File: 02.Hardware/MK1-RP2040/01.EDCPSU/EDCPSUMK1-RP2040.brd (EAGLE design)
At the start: 96 x 53.1 mm, 182 parts, among them J6 Display, Q2 2N7002PW, Q4 2N7002PW, Q9 2N7002PW, U1 RP2040TR7, U11 AP63203, U12 AP64501SP-13, U2 MCP4725, U3 SN74AC14PWR, U4 MAX9938FEUK+T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

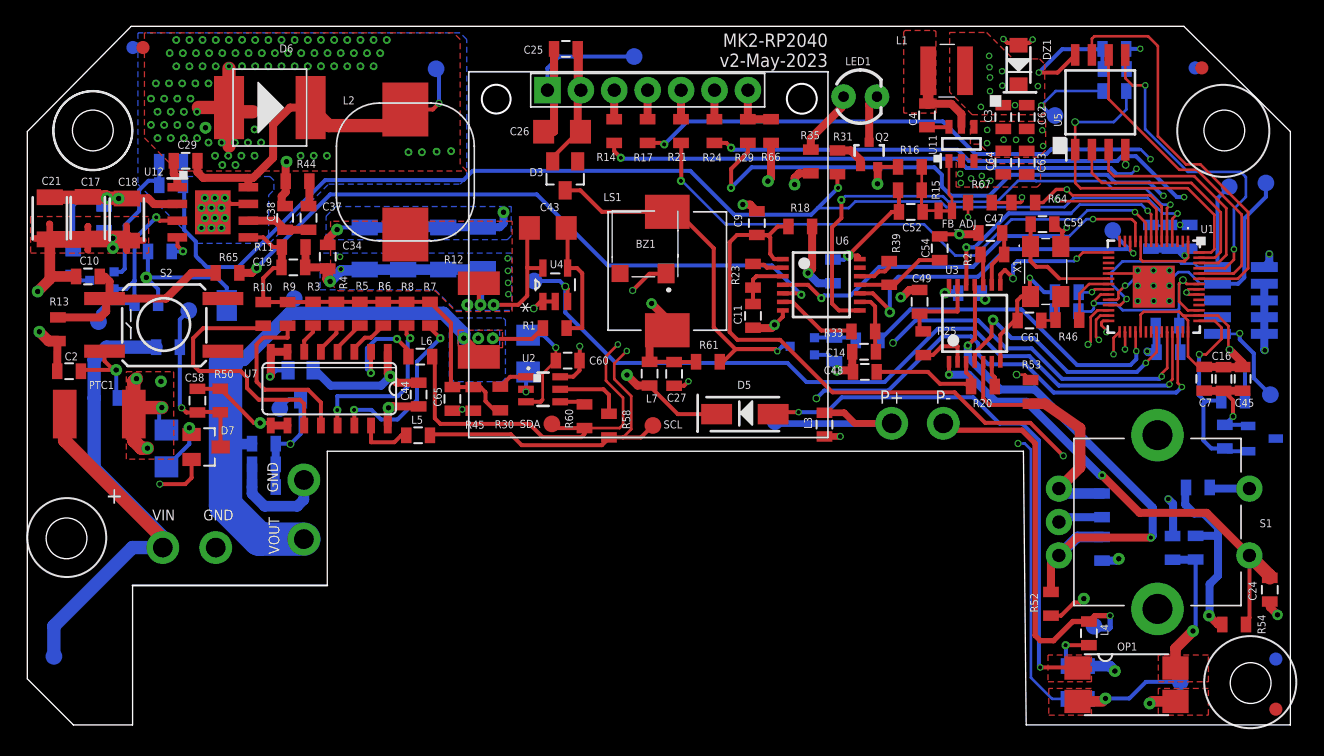
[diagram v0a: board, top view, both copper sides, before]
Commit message: Actualizacion BOM MK1 RP2040 y cambios menores
Se agranda los agujeros laterales del rotary.
Intercambio de posición de las vías del pedal.
Acortamiento de la peninsula.
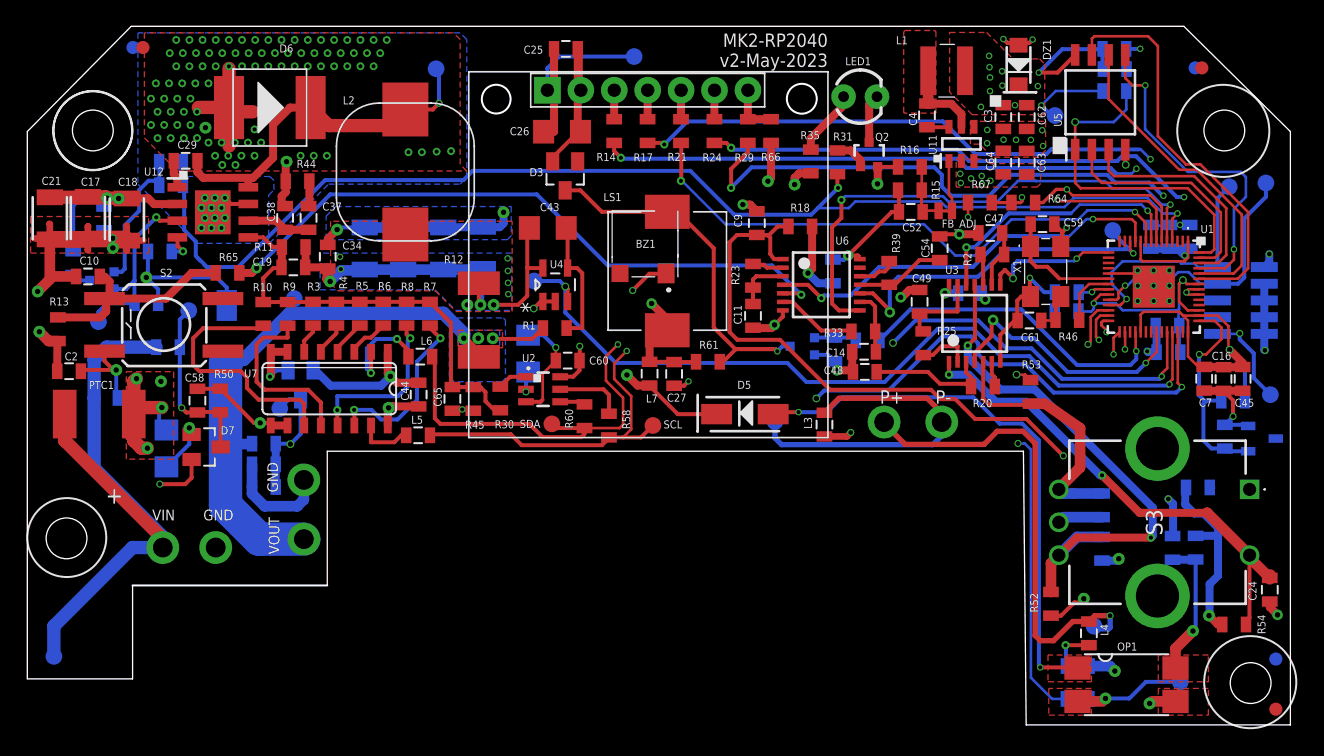
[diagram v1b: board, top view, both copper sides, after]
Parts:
- removed S1: ROTARTY_ENCODER, SparkFun-Electromechanical:ROTARY_ENC_PLAIN
- added S3: PEC12R-3220F-S0024, PEC12R-3220F-S0024:PEC12R3220FS0024
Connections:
- net GND: now also S3.1, S3.C1; no longer S1.C, S1.SW-
- net ROTA: now also S3.A1; no longer S1.A
- net ROTB: now also S3.B1; no longer S1.B
- net ROTPUSH: now also S3.2; no longer S1.SW+
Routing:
- net PEDAL+: track 14.4 -> 26.0 mm
- net PEDAL-: track 31.1 -> 36.5 mm
- net GND: track 210.9 -> 208.0 mm
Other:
- outline, holes or cut-outs redrawn

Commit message: Cierra issue #2 y revision general para peticion de fabricacion SETI
Revision general.
Se añade detalles menores.
Cierra issue #2
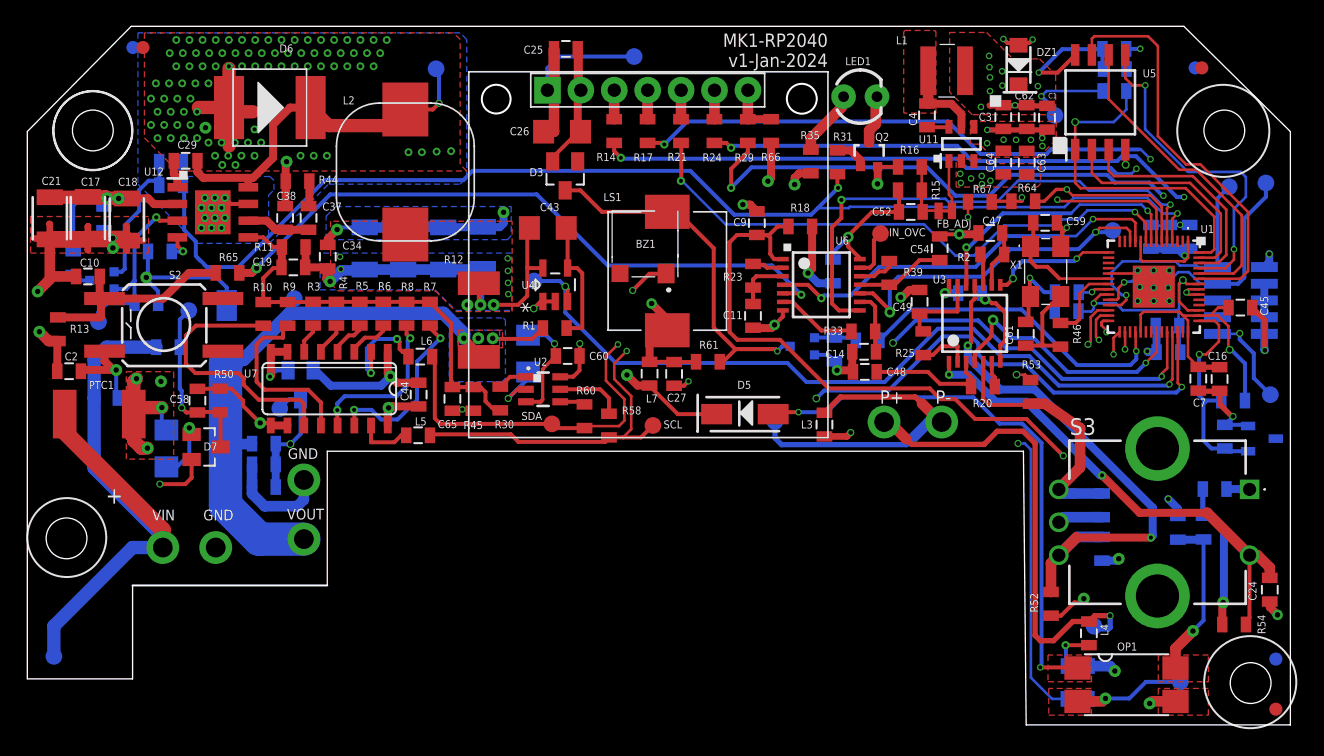
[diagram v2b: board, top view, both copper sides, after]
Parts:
- added C1: 100n 50v X7R/X5R, SparkFun-Passives:0805
- added IN_OVC: TESTPAD_TPSQB1,27, BeagleBone_Blue_R3:TESTPAD_B1,27
- moved C45 5.42 mm to (107.0, 51.4), turned to 0 degrees
- moved R19 1.64 mm to (104.2, 34.7)
- moved R99 1.58 mm to (102.2, 34.7)
- moved C12 1.28 mm to (105.0, 37.6)
- moved R46 1.23 mm to (93.3, 49.4), turned to 270 degrees
- moved C61 1.05 mm to (90.7, 49.4), turned to 270 degrees
- moved C7 0.45 mm to (103.8, 46.0)
- moved C60 0.35 mm to (55.9, 47.7)
- moved C16 0.30 mm to (105.4, 46.0)
- moved C59 0.22 mm to (92.2, 57.9)
- moved R64 0.10 mm to (90.5, 59.5)
- moved R67 0.05 mm to (87.2, 59.5)
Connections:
- net 3V3MCU: now also C1.2
- net GND: now also C1.1
- net IN_OVC: now also IN_OVC.TP
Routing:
- net GND: track 208.0 -> 222.2 mm
- net N$63: track 3.26 -> 7.26 mm
- net IN_OVC: track 0.00 -> 3.71 mm
- net SDA: track 92.4 -> 88.9 mm
- net ROTB: track 44.3 -> 41.3 mm
- net PEDAL: track 10.6 -> 12.6 mm
- net XOUT: track 4.53 -> 6.07 mm
- net PDL: track 56.9 -> 55.5 mm
- net ROTB_FILT: track 10.9 -> 9.62 mm
- net 3V3MCU: track 148.8 -> 149.9 mm
- net N$9: track 19.5 -> 20.5 mm
- net PEDAL+: track 26.0 -> 25.1 mm
- net OVC_ALARM: track 28.2 -> 27.5 mm
- net SS: track 61.5 -> 60.8 mm
- net N$17: track 16.5 -> 15.9 mm
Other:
- board text added: "MK1-RP2040 v1-Jan-2024"
- board text removed: "MK2-RP2040 v2-May-2023"

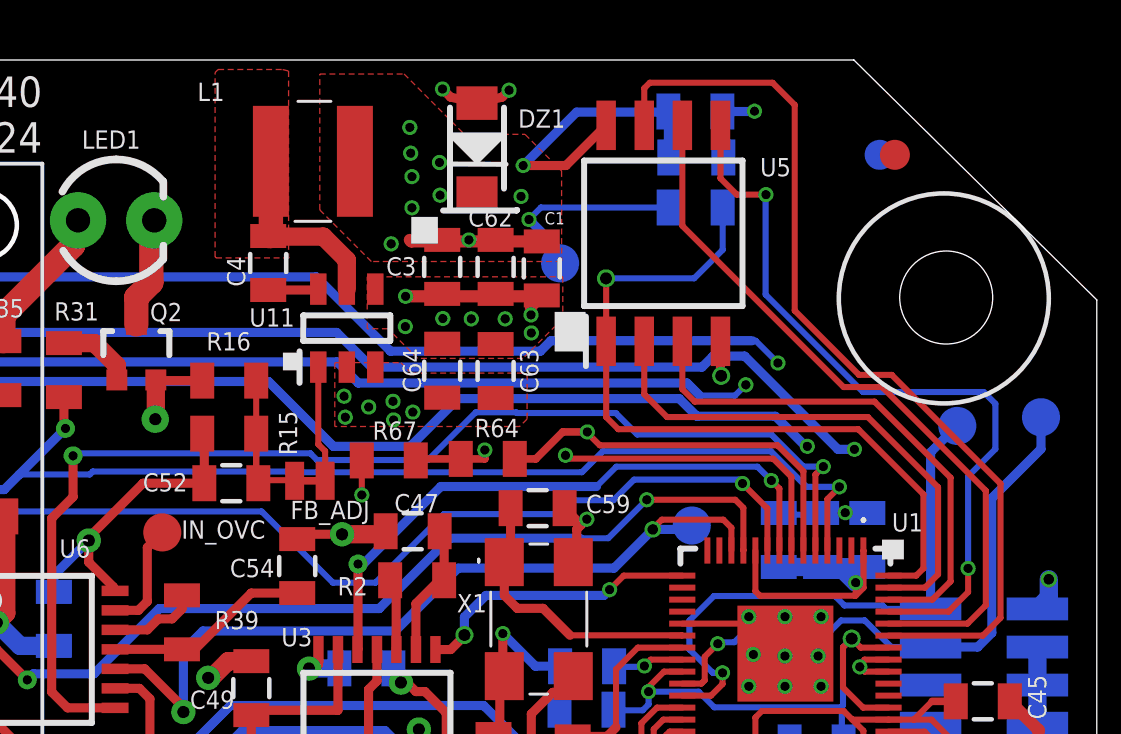
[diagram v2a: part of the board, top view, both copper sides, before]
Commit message: PCB MK1 RP2040- Pines RX TX
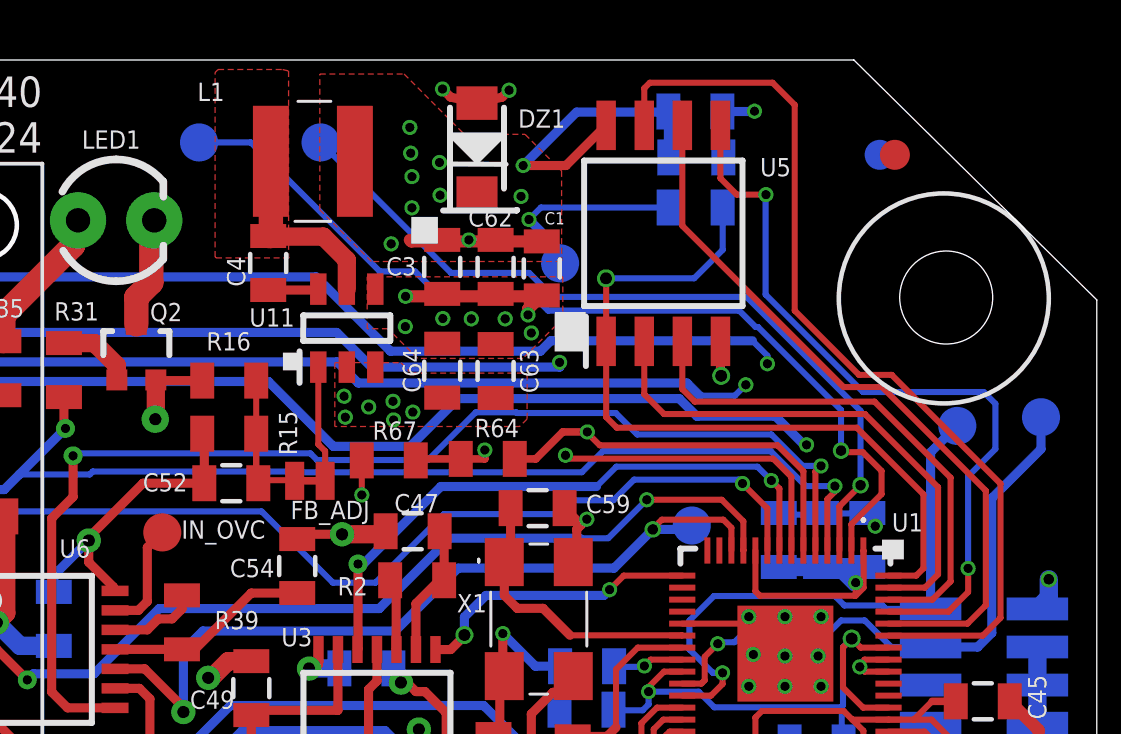
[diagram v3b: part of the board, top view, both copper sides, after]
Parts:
- added RX, TX: TESTPAD_TPSQB1,27, BeagleBone_Blue_R3:TESTPAD_B1,27
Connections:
- net RX: now also RX.TP
- net TX: now also TX.TP
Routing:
- net TX: track 0.00 -> 31.1 mm, vias 0 -> 1
- net RX: track 0.00 -> 26.7 mm, vias 0 -> 1
- net GND: track 222.2 -> 223.2 mm
- net MISO: track 58.5 -> 57.5 mm
